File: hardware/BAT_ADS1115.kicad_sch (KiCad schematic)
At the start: 10 parts, among them J101 INPUTS, J102 OUTPUTS, SW101 SW_Reset, SW102 SSSS811101, U101 ESP32-S3-WROOM-1

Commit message: Tracing 3
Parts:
- removed C101: 1uF, Capacitor_SMD:C_0805_2012Metric, symbol Device:C
- removed J101: INPUTS, TerminalBlock_Phoenix:TerminalBlock_Phoenix_MKDS-1,5-6-5.08_1x06_P5.08mm_Horizontal, symbol Connector:Screw_Terminal_01x06
- removed J102: OUTPUTS, TerminalBlock_Phoenix:TerminalBlock_Phoenix_MKDS-1,5-6-5.08_1x06_P5.08mm_Horizontal, symbol Connector:Screw_Terminal_01x06
- removed R101, R102: 10K, Resistor_SMD:R_0603_1608Metric_Pad0.98x0.95mm_HandSolder, symbol Device:R
- removed R103, R104: 4.7K, Resistor_SMD:R_0603_1608Metric_Pad0.98x0.95mm_HandSolder, symbol Device:R
- removed SW101: SW_Reset, Button_Switch_SMD:SW_Push_SPST_NO_Alps_SKRK, symbol Switch:SW_Push
- removed SW102: SSSS811101, SSSS811101:SW_SSSS811101, symbol NosLib:SSSS811101
- removed U101: ESP32-S3-WROOM-1, PCM_Espressif:ESP32-S3-WROOM-1, symbol PCM_Espressif:ESP32-S3-WROOM-1
- added C201: 1uF, Capacitor_SMD:C_0805_2012Metric, symbol Device:C
- added C202: 100nF, Capacitor_SMD:C_0603_1608Metric, symbol Device:C
- added CN201: C_Pack04, NosLib:C_Array_Convex_4x0603, symbol NosLib:C_Pack04
- added J201: BAT_SENSE, Connector_JST:JST_GH_SM04B-GHS-TB_1x04-1MP_P1.25mm_Horizontal, symbol Connector_Generic_MountingPin:Conn_01x04_MountingPin
- added J202: BAT_NTC, Connector_JST:JST_GH_SM02B-GHS-TB_1x02-1MP_P1.25mm_Horizontal, symbol Connector_Generic_MountingPin:Conn_01x02_MountingPin
- added RN201: 39K, Resistor_SMD:R_Array_Convex_4x0603, symbol Device:R_Pack04
- added RN202: 10K, Resistor_SMD:R_Array_Convex_4x0603, symbol Device:R_Pack04
- added U201: ADS1115IDGS, Package_SO:TSSOP-10_3x3mm_P0.5mm, symbol Analog_ADC:ADS1115IDGS
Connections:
- net +3.3V: now also C202.1, J202.1 (Pin_1), U201.8 (VDD)
- net GND: now also C201.2, C202.2, CN201.5 (C4.1), CN201.6 (C3.1), CN201.7 (C2.1), CN201.8 (C1.1), J201.1 (Pin_1), J201.MP (MountPin), J202.MP (MountPin), RN202.5 (R4.2), RN202.6 (R3.2), RN202.7 (R2.2), RN202.8 (R1.2), U201.3 (GND)
- net SCL: now also U201.10 (SCL)
- net SDA: now also U201.9 (SDA)
- new net: CN201.3 (C3.1), RN201.6 (R3.2), RN202.3 (R3.1), U201.6 (AIN2)
- new net: CN201.2 (C2.1), RN201.7 (R2.2), RN202.2 (R2.1), U201.5 (AIN1)
- new net: CN201.1 (C1.1), RN201.8 (R1.2), RN202.1 (R1.1), U201.4 (AIN0)
- new net: C201.1, CN201.4 (C4.1), J202.2 (Pin_2), RN202.4 (R4.1), U201.7 (AIN3)
- new net ADDR: U201.1 (ADDR)
- new net ALERT: U201.2 (ALERT/RDY)
- new net BAT_1: J201.2 (Pin_2), RN201.1 (R1.1)
- new net BAT_2: J201.3 (Pin_3), RN201.2 (R2.1)
- new net BAT_3: J201.4 (Pin_4), RN201.3 (R3.1)
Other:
- removed sheet BAT_ADS1115
- removed sheet INA226_BAT
- removed sheet INA226_IN
- removed sheet MP2307
- removed sheet Output1
- removed sheet Output2
- removed sheet Output3
- removed sheet USB_LDO
- note removed: "ESP32 EN, BOOT, I2C"
- note removed: "I2C_ADDR=0x40"
- note removed: "I2C_ADDR=0x41"
- note removed: "I2C_ADDR=0x44"
- note removed: "I2C_ADDR=0x45"
- note removed: "I2C_ADDR=0x46"
- note removed: "I2C_ADDR=0x48"
- note removed: "Power Supply"
- title: NosVolt -> (none)

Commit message: Fixes
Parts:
- removed C201: 1uF, Capacitor_SMD:C_0805_2012Metric, symbol Device:C
- added R201: 1K, symbol Device:R
- CN201: value C_Pack04 -> 100nF
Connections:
- net at CN201.4 (C4.1), J202.2 (Pin_2), RN202.4 (R4.1): now also R201.2; no longer U201.7 (AIN3)
- new net: R201.1, U201.7 (AIN3)
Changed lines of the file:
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@@
-	)
-	(junction
-		(at 157.48 123.19)
-		(diameter 0)
-		(color 0 0 0 0)
 	)
 	(junction
@@
 	)
 	(junction
-		(at 157.48 110.49)
-		(diameter 0)
-		(color 0 0 0 0)
-	)
-	(junction
 		(at 144.78 96.52)
 		(diameter 0)
@@
 	(wire
 		(pts
-			(xy 157.48 120.65) (xy 157.48 123.19)
-		)
-		(stroke
-			(width 0)
-			(type default)
-		)
-	)
-	(wire
-		(pts
 			(xy 115.57 101.6) (xy 120.65 101.6)
 		)
@@
 	(wire
 		(pts
-			(xy 162.56 123.19) (xy 157.48 123.19)
+			(xy 152.4 123.19) (xy 162.56 123.19)
 		)
 		(stroke
@@
 	(wire
 		(pts
-			(xy 152.4 80.01) (xy 152.4 110.49)
-		)
-		(stroke
-			(width 0)
-			(type default)
-		)
-	)
-	(wire
-		(pts
-			(xy 152.4 123.19) (xy 157.48 123.19)
-		)
-		(stroke
-			(width 0)
-			(type default)
-		)
-	)
-	(wire
-		(pts
 			(xy 125.73 77.47) (xy 125.73 96.52)
 		)
@@
 	(wire
 		(pts
-			(xy 157.48 110.49) (xy 157.48 113.03)
-		)
-		(stroke
-			(width 0)
-			(type default)
-		)
-	)
-	(wire
-		(pts
 			(xy 194.31 74.93) (xy 200.66 74.93)
 		)
@@
 	(wire
 		(pts
+			(xy 152.4 92.71) (xy 152.4 110.49)
+		)
+		(stroke
+			(width 0)
+			(type default)
+		)
+	)
+	(wire
+		(pts
 			(xy 144.78 123.19) (xy 147.32 123.19)
 		)
@@
 		(pts
 			(xy 147.32 99.06) (xy 147.32 111.76)
+		)
+		(stroke
+			(width 0)
+			(type default)
+		)
+	)
+	(wire
+		(pts
+			(xy 152.4 80.01) (xy 152.4 85.09)
 		)
 		(stroke
@@
 			)
 			(justify left)
+		)
+	)
+	(symbol
+		(lib_id "Device:R")
+		(at 152.4 88.9 0)
+		(unit 1)
+		(exclude_from_sim no)
+		(in_bom yes)
+		(on_board yes)
+		(dnp no)
+		(fields_autoplaced yes)
+		(property "Reference" "R201"
+			(at 154.94 87.6299 0)
+			(effects
+				(font
+					(size 1.27 1.27)
+				)
+				(justify left)
+			)
+		)
+		(property "Value" "1K"
+			(at 154.94 90.1699 0)
+			(effects
+				(font
+					(size 1.27 1.27)
+				)
+				(justify left)
+			)
+		)
+		(property "Footprint" ""
+			(at 150.622 88.9 90)
+			(effects
+				(font
+					(size 1.27 1.27)
+				)
+				(hide yes)
+			)
+		)
+		(property "Datasheet" "~"
+			(at 152.4 88.9 0)
+			(effects
+				(font
+					(size 1.27 1.27)
+				)
+				(hide yes)
+			)
+		)
+		(property "Description" "Resistor"
+			(at 152.4 88.9 0)
+			(effects
+				(font
+					(size 1.27 1.27)
+				)
+				(hide yes)
+			)
+		)
+		(pin "1"
+		)
+		(pin "2"
+		)
+		(instances
+			(project ""
+				(path "/2a3ef4c2-927a-45cd-a4f2-5ee83a7e9444/b91b158d-0995-46c2-acca-efa58b88f071"
+					(reference "R201")
+					(unit 1)
+				)
+			)
 		)
 	)
@@
 			)
 		)
-		(property "Value" "C_Pack04"
+		(property "Value" "100nF"
 			(at 142.24 118.1153 0)
 			(effects
@@
 					(unit 1)
 				)
-			)
-		)
-	)
-	(symbol
-		(lib_id "Device:C")
-		(at 157.48 116.84 0)
-		(unit 1)
-		(exclude_from_sim no)
-		(in_bom yes)
-		(on_board yes)
-		(dnp no)
-		(property "Reference" "C201"
-			(at 161.036 115.824 0)
-			(effects
-				(font
-					(size 1.27 1.27)
-				)
-				(justify left)
-			)
-		)
-		(property "Value" "1uF"
-			(at 161.036 118.364 0)
-			(effects
-				(font
-					(size 1.27 1.27)
-				)
-				(justify left)
-			)
-		)
-		(property "Footprint" "Capacitor_SMD:C_0805_2012Metric"
-			(at 158.4452 120.65 0)
-			(effects
-				(font
-					(size 1.27 1.27)
-				)
-				(hide yes)
-			)
-		)
-		(property "Datasheet" "~"
-			(at 157.48 116.84 0)
-			(effects
-				(font
-					(size 1.27 1.27)
-				)
-				(hide yes)
-			)
-		)
-		(property "Description" "Unpolarized capacitor"
-			(at 157.48 116.84 0)
-			(effects
-				(font
-					(size 1.27 1.27)
-				)
-				(hide yes)
-			)
-		)
-		(pin "1"
-		)
-		(pin "2"
-		)
-		(instances
-			(project "NosVolt"
-				(path "/2a3ef4c2-927a-45cd-a4f2-5ee83a7e9444/b91b158d-0995-46c2-acca-efa58b88f071"
-					(reference "C201")
-					(unit 1)
-				)
-			)
-			(project "BAT_ADS1115"
-				(path "/ddeae9c3-f576-48cb-b110-d894ee9231a1"
-					(reference "C?")
-					(unit 1)
-				)

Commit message: trace ads1115
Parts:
- R201: footprint (none) -> Resistor_SMD:R_0603_1608Metric_Pad0.98x0.95mm_HandSolder
- renumbered C202 to C201
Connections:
- net at R201.1, U201.7 (AIN3): now also CN201.1 (C1.1)
- net at J202.2 (Pin_2), R201.2, RN202.4 (R4.1): no longer CN201.4 (C4.1)
- net at RN201.6 (R3.2), RN202.3 (R3.1), U201.6 (AIN2): now also CN201.2 (C2.1); no longer CN201.3 (C3.1)
- net at RN201.7 (R2.2), RN202.2 (R2.1), U201.5 (AIN1): now also CN201.3 (C3.1); no longer CN201.2 (C2.1)
- net at RN201.8 (R1.2), RN202.1 (R1.1), U201.4 (AIN0): now also CN201.4 (C4.1); no longer CN201.1 (C1.1)
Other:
- moved on the sheet: CN201

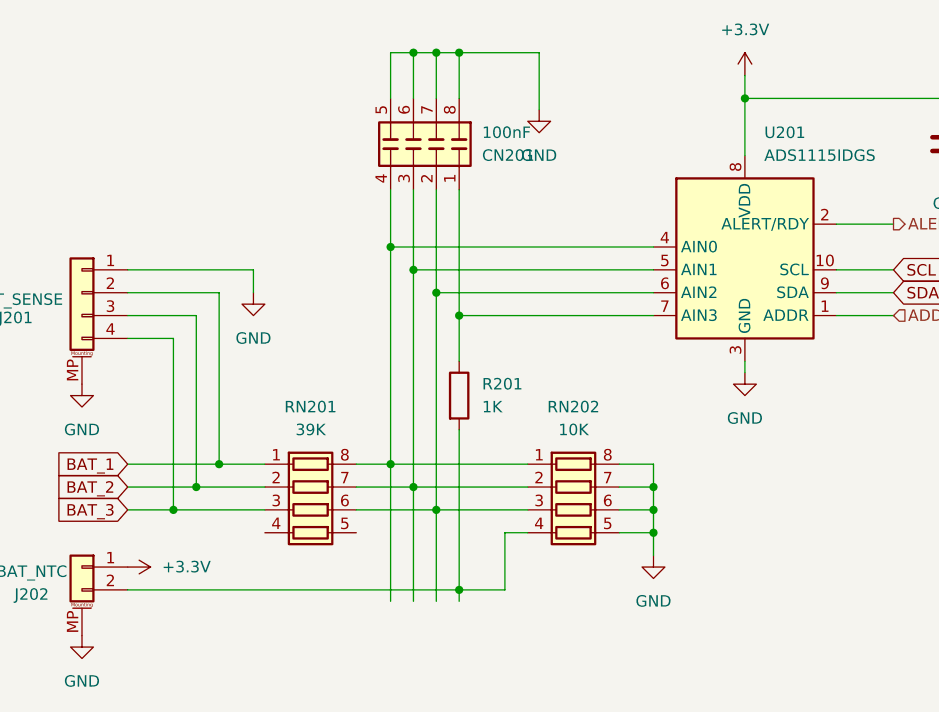
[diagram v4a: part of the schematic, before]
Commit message: thermal relief
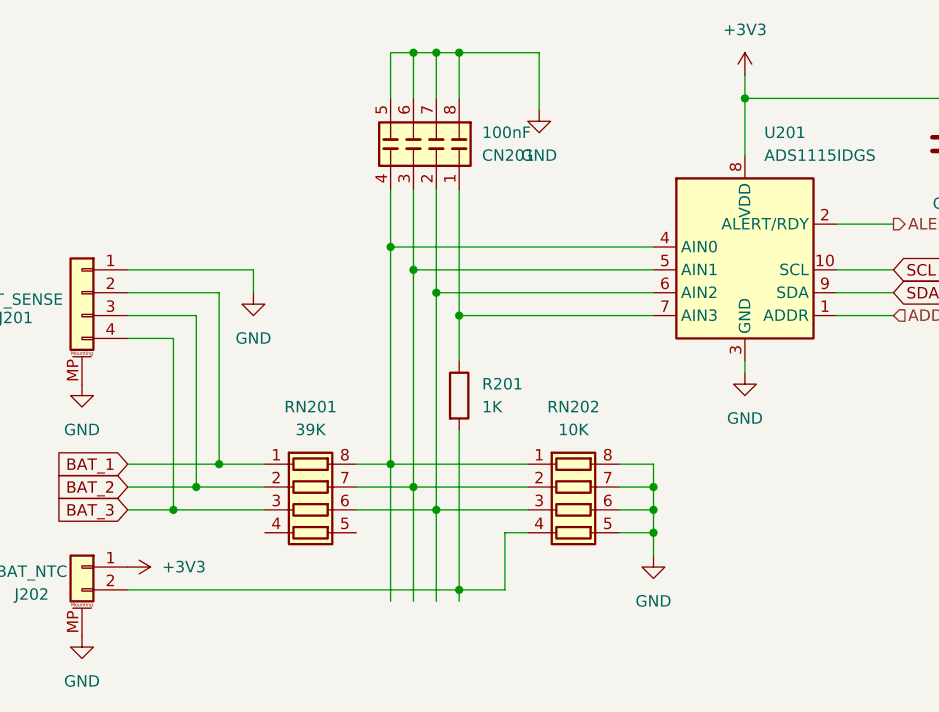
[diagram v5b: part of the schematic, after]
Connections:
- net +3.3V renamed +3V3
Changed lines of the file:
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@@
 			)
 		)
-		(property "Value" "+3.3V"
+		(property "Value" "+3V3"
 			(at 184.15 48.26 0)
 			(effects
@@
 			)
 		)
-		(property "Value" "+3.3V"
+		(property "Value" "+3V3"
 			(at 119.38 107.9499 90)
 			(effects

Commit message: Test points
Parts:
- removed J202: BAT_NTC, Connector_JST:JST_GH_SM02B-GHS-TB_1x02-1MP_P1.25mm_Horizontal, symbol Connector_Generic_MountingPin:Conn_01x02_MountingPin
- removed R201: 1K, Resistor_SMD:R_0603_1608Metric_Pad0.98x0.95mm_HandSolder, symbol Device:R
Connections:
- net GND: no longer RN202.5 (R4.2)
- net at U201.7 (AIN3): no longer CN201.1 (C1.1)
- no-connect marks 0 -> 4

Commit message: hand soldering footprints and led
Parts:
- C201: footprint Capacitor_SMD:C_0603_1608Metric -> Capacitor_SMD:C_0603_1608Metric_Pad1.08x0.95mm_HandSolder
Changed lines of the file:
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@@
 			)
 		)
-		(property "Footprint" "Capacitor_SMD:C_0603_1608Metric"
+		(property "Footprint" "Capacitor_SMD:C_0603_1608Metric_Pad1.08x0.95mm_HandSolder"
 			(at 207.9752 64.77 0)
 			(effects

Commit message: PWR_FLG
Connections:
- net BAT_1 renamed BAT1
- net BAT_2 renamed BAT2
- net BAT_3 renamed BAT3
- no-connect marks 4 -> 6
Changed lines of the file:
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@@
+	)
+	(no_connect
+		(at 152.4 66.04)
 	)
 	(no_connect
@@
 	)
 	(no_connect
+		(at 173.99 80.01)
+	)
+	(no_connect
 		(at 130.81 104.14)
 	)
@@
 	(wire
 		(pts
-			(xy 115.57 101.6) (xy 120.65 101.6)
+			(xy 110.49 101.6) (xy 120.65 101.6)
 		)
 		(stroke
@@
 	(wire
 		(pts
-			(xy 115.57 99.06) (xy 123.19 99.06)
-		)
-		(stroke
-			(width 0)
-			(type default)
-		)
-	)
-	(wire
-		(pts
 			(xy 194.31 77.47) (xy 200.66 77.47)
 		)
@@
 	(wire
 		(pts
-			(xy 115.57 96.52) (xy 125.73 96.52)
+			(xy 110.49 96.52) (xy 125.73 96.52)
 		)
 		(stroke
@@
 	(wire
 		(pts
+			(xy 110.49 99.06) (xy 123.19 99.06)
+		)
+		(stroke
+			(width 0)
+			(type default)
+		)
+	)
+	(wire
+		(pts
 			(xy 149.86 101.6) (xy 160.02 101.6)
 		)
@@
 	(wire
 		(pts
-			(xy 144.78 96.52) (xy 144.78 111.76)
-		)
-		(stroke
-			(width 0)
-			(type default)
-		)
-	)
-	(wire
-		(pts
 			(xy 120.65 82.55) (xy 120.65 101.6)
 		)
@@
 	(wire
 		(pts
-			(xy 152.4 80.01) (xy 173.99 80.01)
-		)
-		(stroke
-			(width 0)
-			(type default)
-		)
-	)
-	(wire
-		(pts
 			(xy 144.78 50.8) (xy 147.32 50.8)
 		)
@@
 	(wire
 		(pts
-			(xy 147.32 99.06) (xy 147.32 111.76)
-		)
-		(stroke
-			(width 0)
-			(type default)
-		)
-	)
-	(wire
-		(pts
 			(xy 194.31 69.85) (xy 200.66 69.85)
 		)
@@
 	(wire
 		(pts
-			(xy 149.86 101.6) (xy 149.86 111.76)
-		)
-		(stroke
-			(width 0)
-			(type default)
-		)
-	)
-	(wire
-		(pts
 			(xy 144.78 96.52) (xy 144.78 72.39)
 		)
@@
 			(width 0)
 			(type default)
+		)
+	)
+	(label "BAT1"
+		(at 110.49 96.52 0)
+		(effects
+			(font
+				(size 1.27 1.27)
+			)
+			(justify left bottom)
+		)
+	)
+	(label "BAT2"
+		(at 110.49 99.06 0)
+		(effects
+			(font
+				(size 1.27 1.27)
+			)
+			(justify left bottom)
+		)
+	)
+	(label "BAT3"
+		(at 110.49 101.6 0)
+		(effects
+			(font
+				(size 1.27 1.27)
+			)
+			(justify left bottom)
 		)
 	)
@@
 				)
 				(justify left)
-				(hide yes)
-			)
-		)
-	)
-	(global_label "BAT_1"
-		(shape input)
-		(at 115.57 96.52 180)
-		(fields_autoplaced yes)
-		(effects
-			(font
-				(size 1.27 1.27)
-			)
-			(justify right)
-		)
-		(property "Intersheetrefs" "${INTERSHEET_REFS}"
-			(at 107.0815 96.52 0)
-			(effects
-				(font
-					(size 1.27 1.27)
-				)
-				(justify right)
-				(hide yes)
-			)
-		)
-	)
-	(global_label "BAT_2"
-		(shape input)
-		(at 115.57 99.06 180)
-		(fields_autoplaced yes)
-		(effects
-			(font
-				(size 1.27 1.27)
-			)
-			(justify right)
-		)
-		(property "Intersheetrefs" "${INTERSHEET_REFS}"
-			(at 107.0815 99.06 0)
-			(effects
-				(font
-					(size 1.27 1.27)
-				)
-				(justify right)
-				(hide yes)
-			)
-		)
-	)
-	(global_label "BAT_3"
-		(shape input)
-		(at 115.57 101.6 180)
-		(fields_autoplaced yes)
-		(effects
-			(font
-				(size 1.27 1.27)
-			)
-			(justify right)
-		)
-		(property "Intersheetrefs" "${INTERSHEET_REFS}"
-			(at 107.0815 101.6 0)
-			(effects
-				(font
-					(size 1.27 1.27)
-				)
-				(justify right)
 				(hide yes)
 			)
@@
 			)
 		)
-		(property "Datasheet" "https://www.ti.com/lit/ds/symlink/ads1115.pdf"
+		(property "Datasheet" "http://www.ti.com/lit/ds/symlink/ads1113.pdf"
 			(at 182.88 97.79 0)
 			(effects
